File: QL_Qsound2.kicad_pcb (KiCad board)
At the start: 2 copper layers, 92.7 x 99.1 mm, 39 parts, among them J1 QL_SLOT_DIN41612_CARD, J2 AudioJack2_Ground_Switch, J3 Conn_02x17_Odd_Even, Q1 2N2369, U1 7805, U2 W27C512, U3 74LS266, U4 6821, U5 LM358, U6 GAL22V10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

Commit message: ADD NOTE
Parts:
- X1, X1B1: value 2Mhz -> 4Mhz
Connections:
- net /RW renamed /WRL
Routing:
- net /A14: track 63.3 -> 54.9 mm
- net /E: track 119.3 -> 124.3 mm
- net /A15: track 67.0 -> 64.3 mm
- net GND: track 445.2 -> 447.3 mm
- net /MEM_SEL: track 53.8 -> 52.1 mm
- net /WRL: track 43.7 -> 42.8 mm
- net /BDIR: track 51.4 -> 50.7 mm

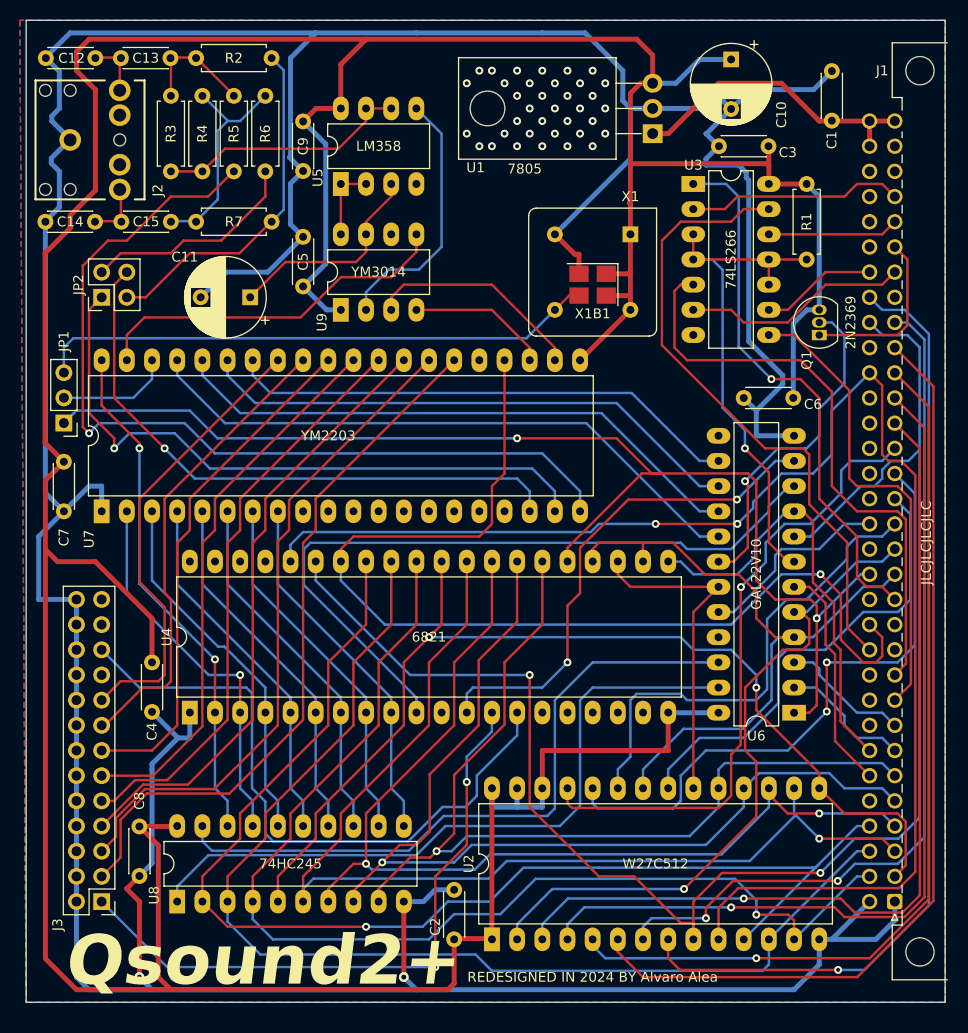
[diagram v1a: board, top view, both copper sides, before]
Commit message: new clock oscilators
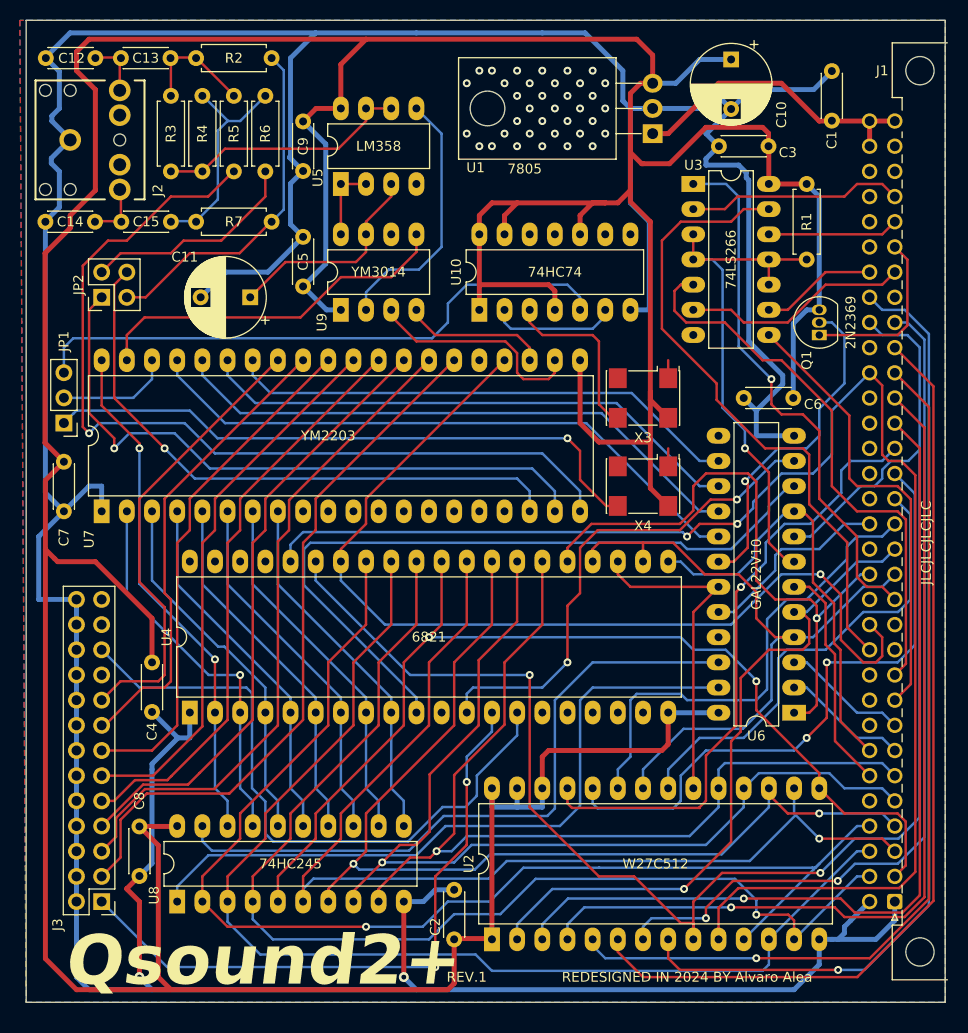
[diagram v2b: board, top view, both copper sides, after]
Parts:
- removed X1: 4Mhz, Oscillator:Oscillator_DIP-8
- added U10: 74HC74, Package_DIP:DIP-14_W7.62mm_LongPads, F.Cu at (148.6, 72.4)
- added X3: 3Mhz, Oscillator:Oscillator_SMD_Abracon_ASV-4Pin_7.0x5.1mm, F.Cu at (165.1, 81.3)
- X4: renamed from X1B1; footprint Oscillator:Oscillator_SMD_Abracon_ASE-4Pin_3.2x2.5mm_HandSoldering -> Oscillator:Oscillator_SMD_Abracon_ASV-4Pin_7.0x5.1mm
- moved X4 20.9 mm to (165.1, 90.2)
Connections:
- JP1 pad 1: /E -> Net-(JP1-A)
- X4 pad 1: VCC -> unconnected-(X4-Vctrl-Pad1)
- X4 pad 3: Net-(JP1-B) -> Net-(JP1-A)
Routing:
- net VCC: track 427.2 -> 502.6 mm
- net Net-(JP1-A): track 0.00 -> 62.1 mm, vias 0 -> 1
- net /E: track 124.3 -> 62.3 mm, vias 2 -> 1
- net Net-(U10A-C): track 0.00 -> 17.3 mm
- net Net-(U10A-D): track 0.00 -> 12.2 mm
- net /RESET: track 105.4 -> 97.9 mm
- net Net-(JP1-B): track 56.7 -> 60.1 mm
- net /A16: track 60.1 -> 56.8 mm
- net unconnected-(X4-Vctrl-Pad1): track 0.00 -> 1.81 mm
- net unconnected-(X3-Vctrl-Pad1): track 0.00 -> 1.81 mm
- net GND: track 447.3 -> 449.0 mm
- net /A17: track 47.3 -> 45.8 mm
- net /A8: track 64.0 -> 62.9 mm
- net /A19: track 13.3 -> 12.8 mm
- net /D5: track 101.3 -> 101.8 mm
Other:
- board text added: "REV.1"

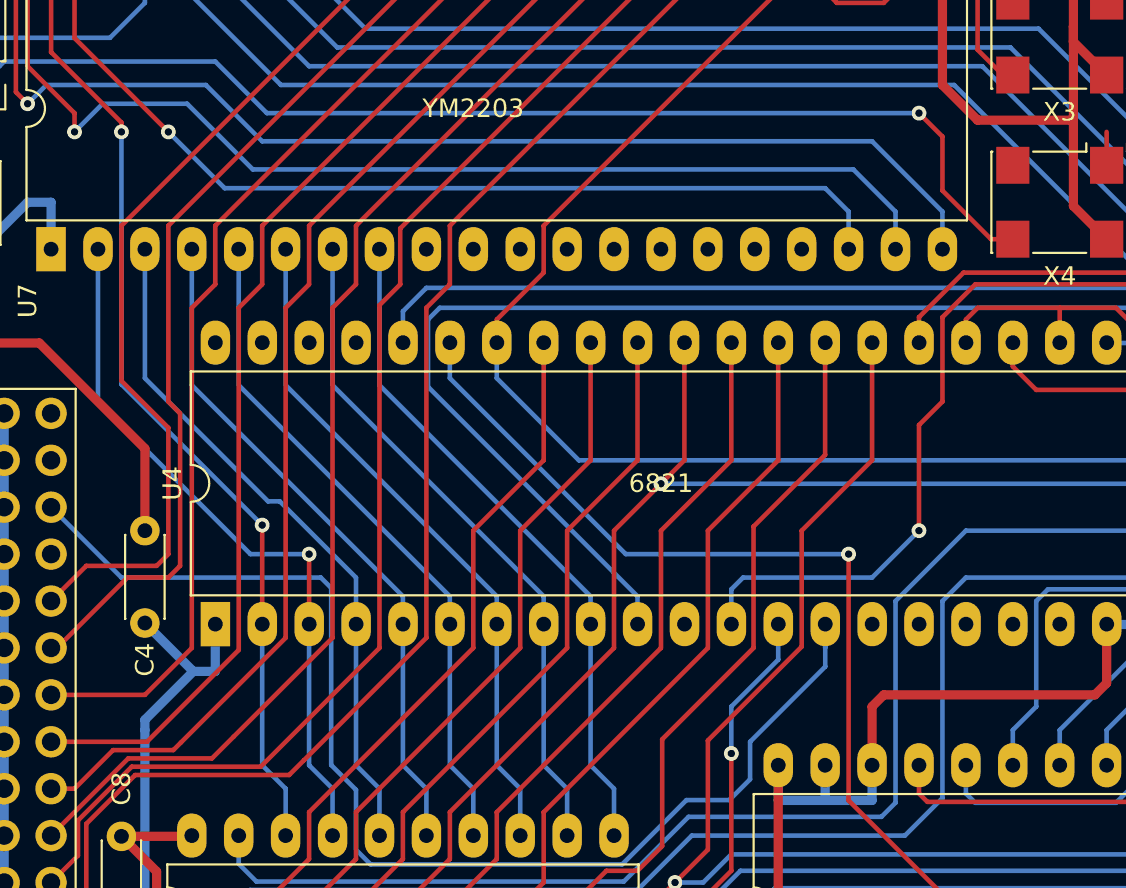
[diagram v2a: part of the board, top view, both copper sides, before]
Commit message: new clock oscilators
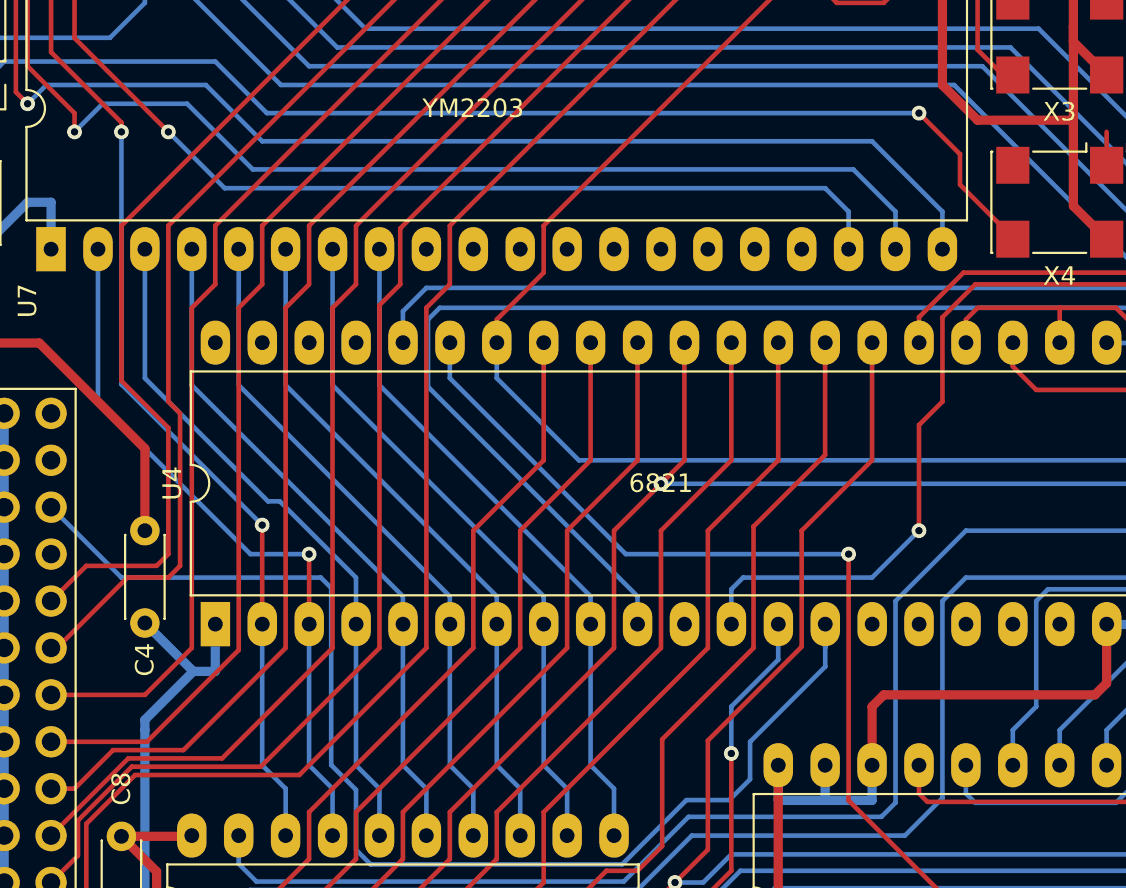
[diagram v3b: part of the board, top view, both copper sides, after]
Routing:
- net Net-(JP1-A): track 62.1 -> 61.3 mm
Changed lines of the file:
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@@
 	)
 	(segment
-		(start 112.396396 123.826396)
-		(end 112.396396 127.633604)
-		(width 0.25)
-		(layer "F.Cu")
-		(net 60)
-	)
-	(segment
-		(start 146.05 77.47)
-		(end 132.08 91.44)
+		(start 130.81 95.885)
+		(end 130.81 114.3)
 		(width 0.25)
 		(layer "F.Cu")
@@
 	)
 	(segment
-		(start 115.042792 121.18)
-		(end 112.396396 123.826396)
+		(start 112.396396 127.633604)
+		(end 110.49 129.54)
 		(width 0.25)
 		(layer "F.Cu")
@@
 	)
 	(segment
-		(start 130.81 113.751)
-		(end 124.185 120.375)
+		(start 146.05 77.47)
+		(end 132.08 91.44)
 		(width 0.25)
 		(layer "F.Cu")
@@
 	)
 	(segment
-		(start 124.185 120.375)
-		(end 123.38 121.18)
+		(start 130.81 114.3)
+		(end 123.93 121.18)
 		(width 0.25)
 		(layer "F.Cu")
@@
 	)
 	(segment
-		(start 130.81 95.885)
-		(end 130.81 113.751)
+		(start 123.93 121.18)
+		(end 115.042792 121.18)
 		(width 0.25)
 		(layer "F.Cu")
@@
 	)
 	(segment
-		(start 112.396396 127.633604)
-		(end 110.49 129.54)
+		(start 115.042792 121.18)
+		(end 112.396396 123.826396)
 		(width 0.25)
 		(layer "F.Cu")
@@
 	)
 	(segment
-		(start 132.08 94.615)
-		(end 130.81 95.885)
+		(start 112.396396 123.826396)
+		(end 112.396396 127.633604)
 		(width 0.25)
 		(layer "F.Cu")
@@
 	)
 	(segment
-		(start 123.38 121.18)
-		(end 115.042792 121.18)
+		(start 132.08 94.615)
+		(end 130.81 95.885)
 		(width 0.25)
 		(layer "F.Cu")
@@
 	)
 	(segment
-		(start 125.73 95.885)
-		(end 125.73 113.751)
+		(start 125.73 114.3)
+		(end 119.75 120.28)
 		(width 0.25)
 		(layer "F.Cu")
@@
 	)
 	(segment
-		(start 127 91.44)
-		(end 127 94.615)
-		(width 0.25)
-		(layer "F.Cu")
-		(net 64)
-	)
-	(segment
-		(start 120.375131 119.105131)
-		(end 119.200262 120.28)
-		(width 0.25)
-		(layer "F.Cu")
-		(net 64)
-	)
-	(segment
-		(start 119.200262 120.28)
+		(start 119.75 120.28)
 		(end 114.67 120.28)
 		(width 0.25)
@@
 	)
 	(segment
-		(start 125.73 113.751)
-		(end 120.375131 119.105131)
+		(start 127 91.44)
+		(end 127 94.615)
 		(width 0.25)
 		(layer "F.Cu")
@@
 	)
 	(segment
-		(start 111.76 121.92)
-		(end 110.49 121.92)
+		(start 125.73 95.885)
+		(end 125.73 114.3)
 		(width 0.25)
 		(layer "F.Cu")
-		(net 65)
+		(net 64)
 	)
 	(segment
-		(start 117.517572 119.422572)
-		(end 117.110144 119.83)
+		(start 123.19 95.885)
+		(end 123.19 114.3)
 		(width 0.25)
 		(layer "F.Cu")
@@
 	)
 	(segment
-		(start 124.46 91.44)
-		(end 124.46 94.615)
+		(start 117.66 119.83)
+		(end 113.85 119.83)
 		(width 0.25)
 		(layer "F.Cu")
@@
 	)
 	(segment
-		(start 117.110144 119.83)
-		(end 113.85 119.83)
+		(start 138.43 77.47)
+		(end 124.46 91.44)
 		(width 0.25)
 		(layer "F.Cu")
@@
 	)
 	(segment
-		(start 124.46 94.615)
-		(end 123.19 95.885)
+		(start 111.76 121.92)
+		(end 110.49 121.92)
 		(width 0.25)
 		(layer "F.Cu")
@@
 	)
 	(segment
-		(start 113.85 119.83)
-		(end 111.76 121.92)
+		(start 123.19 114.3)
+		(end 117.66 119.83)
 		(width 0.25)
 		(layer "F.Cu")
@@
 	)
 	(segment
-		(start 138.43 77.47)
-		(end 124.46 91.44)
+		(start 124.46 91.44)
+		(end 124.46 94.615)
 		(width 0.25)
 		(layer "F.Cu")
@@
 	)
 	(segment
-		(start 123.19 95.885)
-		(end 123.19 113.751)
+		(start 124.46 94.615)
+		(end 123.19 95.885)
 		(width 0.25)
 		(layer "F.Cu")
@@
 	)
 	(segment
-		(start 123.19 113.751)
-		(end 117.517572 119.422572)
+		(start 113.85 119.83)
+		(end 111.76 121.92)
 		(width 0.25)
 		(layer "F.Cu")
@@
 	)
 	(segment
-		(start 158.75 86.614)
-		(end 158.75 89.535)
-		(width 0.25)
-		(layer "F.Cu")
-		(net 136)
-	)
-	(segment
-		(start 161.385 92.17)
-		(end 158.75 89.535)
+		(start 159.7025 89.2175)
+		(end 159.7025 87.5665)
 		(width 0.25)
 		(layer "F.Cu")
@@
 	)
 	(segment
-		(start 157.48 85.344)
-		(end 158.75 86.614)
+		(start 159.7025 87.5665)
+		(end 157.48 85.344)
 		(width 0.25)
 		(layer "F.Cu")
@@
 	)
 	(segment
-		(start 162.56 92.17)
-		(end 161.385 92.17)
+		(start 162.56 92.075)
+		(end 159.7025 89.2175)
 		(width 0.25)
 		(layer "F.Cu")
